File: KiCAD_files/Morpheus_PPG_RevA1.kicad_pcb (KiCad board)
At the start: 2 copper layers, 52.8 x 29.7 mm, 33 parts, among them P1 CONN_01X01, P10 CONN_01X04, P11 CONN_01X01, P12 CONN_01X04, P13 CONN_01X01, P14 CONN_01X01, P2 CONN_01X01, P3 CONN_01X01, P4 CONN_01X01, P5 CONN_01X01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

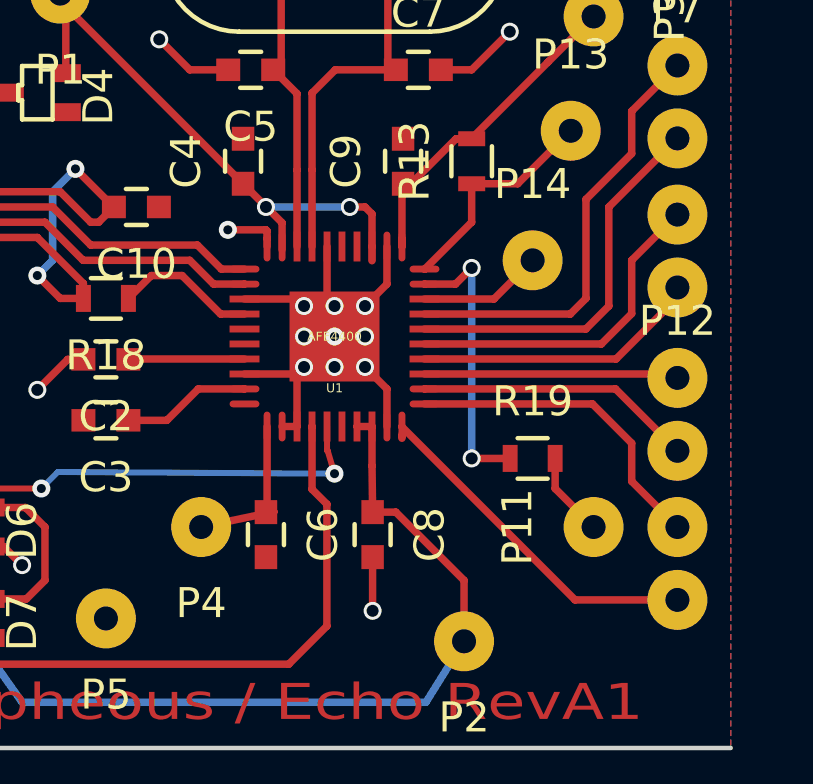
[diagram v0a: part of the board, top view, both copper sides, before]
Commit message: Copper traces for silk screen
Minor corrections (GND) + alignment traces on the corners of AFE4400
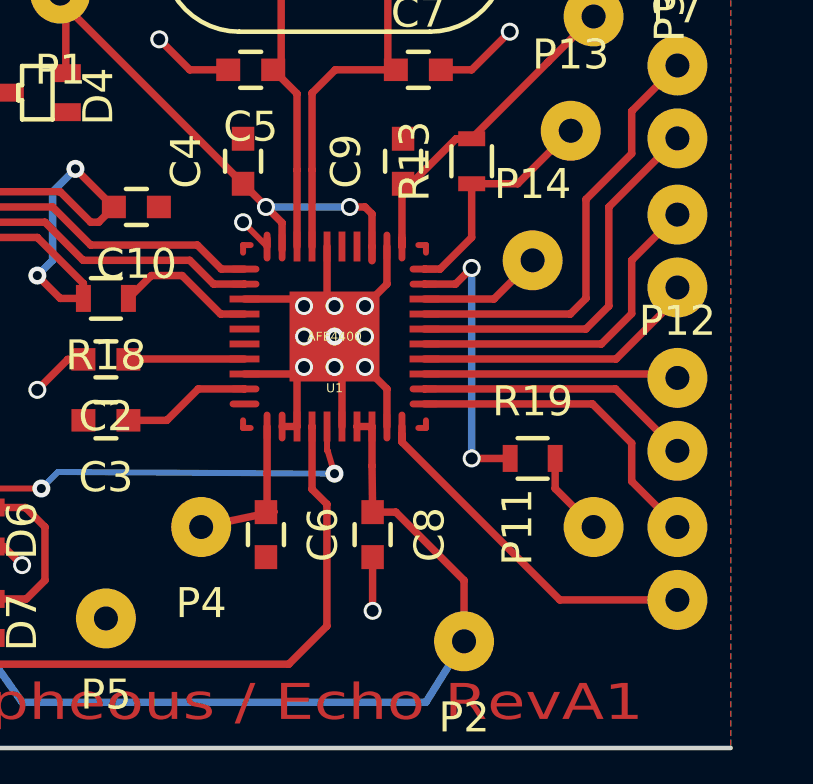
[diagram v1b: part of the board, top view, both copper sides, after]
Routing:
- net GND: track 41.5 -> 44.2 mm
- net (no net): track 8.83 -> 10.9 mm
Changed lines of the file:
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@@
     (thickness 1.6)
     (drawings 15)
-    (tracks 391)
+    (tracks 400)
     (zones 0)
     (modules 33)
@@
       (padsonsilk false)
       (subtractmaskfromsilk false)
-      (outputformat 1)
+      (outputformat 4)
       (mirror false)
       (drillshape 0)
@@
     (effects (font (size 1.5 1.5) (thickness 0.3)))
   )
+  (segment (start 145.542 103.124) (end 145.542 102.87) (width 0.2) (layer F.Cu) (net 0))
+  (segment (start 145.542 102.87) (end 145.288 102.87) (width 0.2) (layer F.Cu) (net 0))
+  (segment (start 145.288 108.966) (end 145.542 108.966) (width 0.2) (layer F.Cu) (net 0))
+  (segment (start 145.542 108.966) (end 145.542 108.712) (width 0.2) (layer F.Cu) (net 0))
   (segment (start 105.58 102.832) (end 104.94 102.832) (width 0.25) (layer F.Cu) (net 0))
   (segment (start 104.902 105.664) (end 104.902 106.172) (width 0.25) (layer F.Cu) (net 0))
@@
   (segment (start 139.4942 108.166) (end 139.4943 108.1659) (width 0.2) (layer F.Cu) (net 0) (status 30))
   (segment (start 139.494 108.166) (end 139.4942 108.166) (width 0.2) (layer F.Cu) (net 0) (status 30))
+  (segment (start 139.7 108.966) (end 139.446 108.966) (width 0.2) (layer F.Cu) (net 0))
+  (segment (start 139.446 108.966) (end 139.446 108.712) (width 0.2) (layer F.Cu) (net 0))
+  (segment (start 139.446 103.124) (end 139.446 102.87) (width 0.2) (layer F.Cu) (net 0))
+  (segment (start 139.446 102.87) (end 139.7 102.87) (width 0.2) (layer F.Cu) (net 0))
   (segment (start 139.49426 106.6673) (end 135.6367 106.6673) (width 0.25) (layer F.Cu) (net 1))
   (segment (start 135.6367 106.6673) (end 135.624 106.68) (width 0.25) (layer F.Cu) (net 1))
   (segment (start 139.494 106.667) (end 139.4943 106.6673) (width 0.2) (layer F.Cu) (net 1) (status 30))
-  (segment (start 130.99796 112.91824) (end 131.46024 112.91824) (width 0.25) (layer F.Cu) (net 2) (status C00000))
-  (segment (start 131.46024 112.91824) (end 132.08 113.538) (width 0.25) (layer F.Cu) (net 2) (status 400000))
+  (segment (start 140.2461 102.91826) (end 139.49426 102.15626) (width 0.2) (layer F.Cu) (net 2))
+  (via (at 139.446 102.108) (size 0.6) (drill 0.4) (layers F.Cu B.Cu) (net 2))
+  (segment (start 139.49426 102.15626) (end 139.446 102.108) (width 0.2) (layer F.Cu) (net 2))
+  (segment (start 142.74292 108.91774) (end 142.74292 106.16692) (width 0.25) (layer F.Cu) (net 2))
+  (segment (start 142.74292 106.16692) (end 142.494 105.918) (width 0.25) (layer F.Cu) (net 2))
+  (segment (start 130.99796 112.91824) (end 131.46024 112.91824) (width 0.25) (layer F.Cu) (net 2))
+  (segment (start 131.46024 112.91824) (end 132.08 113.538) (width 0.25) (layer F.Cu) (net 2))
   (via (at 132.08 113.538) (size 0.6) (drill 0.4) (layers F.Cu B.Cu) (net 2))
   (segment (start 134.124 106.68) (end 133.604 106.68) (width 0.25) (layer F.Cu) (net 2))
@@
   (via (at 141.478 104.902) (size 0.6) (drill 0.4) (layers F.Cu B.Cu) (net 2) (status 30))
   (segment (start 141.478 104.902) (end 142.494 105.918) (width 0.25) (layer F.Cu) (net 2) (status 30))
-  (via (at 138.938 102.362) (size 0.6) (layers F.Cu B.Cu) (net 2))
   (via (at 142.494 105.918) (size 0.6) (layers F.Cu B.Cu) (net 2) (status 30))
-  (segment (start 140.208 102.362) (end 138.938 102.362) (width 0.25) (layer F.Cu) (net 2))
-  (segment (start 140.246 102.4) (end 140.208 102.362) (width 0.25) (layer F.Cu) (net 2))
-  (segment (start 140.246 102.654) (end 140.246 102.4) (width 0.25) (layer F.Cu) (net 2) (status 10))
   (segment (start 140.246 102.918) (end 140.246 102.654) (width 0.2) (layer F.Cu) (net 2) (status 30))
   (segment (start 142.743 106.167) (end 142.494 105.918) (width 0.25) (layer F.Cu) (net 2) (status 30))
@@
   (segment (start 141.7447 100.3608) (end 141.7447 102.9183) (width 0.2) (layer F.Cu) (net 7) (status 20))
   (segment (start 141.745 100.3605) (end 141.7447 100.3608) (width 0.2) (layer F.Cu) (net 7))
-  (segment (start 130.99796 111.61776) (end 132.19176 111.61776) (width 0.25) (layer F.Cu) (net 8) (status 400000))
-  (segment (start 132.22224 114.66576) (end 130.99796 114.66576) (width 0.25) (layer F.Cu) (net 8) (status 800000))
+  (segment (start 130.99796 111.61776) (end 132.19176 111.61776) (width 0.25) (layer F.Cu) (net 8))
+  (segment (start 132.22224 114.66576) (end 130.99796 114.66576) (width 0.25) (layer F.Cu) (net 8))
   (segment (start 132.842 114.046) (end 132.22224 114.66576) (width 0.25) (layer F.Cu) (net 8))
   (segment (start 132.842 112.268) (end 132.842 114.046) (width 0.25) (layer F.Cu) (net 8))
@@
   (segment (start 153.924 104.902) (end 153.924 104.538) (width 0.25) (layer F.Cu) (net 14) (status 30))
   (segment (start 145.494 106.667) (end 145.4937 106.6673) (width 0.2) (layer F.Cu) (net 14) (status 30))
+  (segment (start 145.49374 103.6701) (end 146.0119 103.6701) (width 0.25) (layer F.Cu) (net 15))
+  (segment (start 147.066 102.616) (end 147.066 100.826) (width 0.25) (layer F.Cu) (net 15))
+  (segment (start 146.0119 103.6701) (end 147.066 102.616) (width 0.25) (layer F.Cu) (net 15))
   (segment (start 147.066 100.826) (end 148.602 100.826) (width 0.25) (layer F.Cu) (net 15))
   (segment (start 148.602 100.826) (end 150.368 99.06) (width 0.25) (layer F.Cu) (net 15) (status 20))
   (segment (start 145.49374 103.6701) (end 145.5039 103.6701) (width 0.25) (layer F.Cu) (net 15))
-  (segment (start 145.5039 103.6701) (end 147.066 102.108) (width 0.25) (layer F.Cu) (net 15))
-  (segment (start 147.066 102.108) (end 147.066 100.826) (width 0.25) (layer F.Cu) (net 15))
   (segment (start 145.494 103.67) (end 145.504 103.67) (width 0.25) (layer F.Cu) (net 15) (status 30))
   (segment (start 145.4938 103.67) (end 145.4937 103.6701) (width 0.2) (layer F.Cu) (net 15) (status 30))
@@
   (segment (start 151.0919 108.1659) (end 152.4 109.474) (width 0.25) (layer F.Cu) (net 19))
   (segment (start 153.67 112.522) (end 153.924 112.268) (width 0.25) (layer F.Cu) (net 19) (status 30))
-  (segment (start 144.7419 108.91774) (end 144.7419 108.9279) (width 0.25) (layer F.Cu) (net 20))
-  (segment (start 144.7419 108.9279) (end 150.512 114.698) (width 0.25) (layer F.Cu) (net 20))
-  (segment (start 150.512 114.698) (end 153.924 114.698) (width 0.25) (layer F.Cu) (net 20))
+  (segment (start 144.7419 108.91774) (end 144.7419 109.4359) (width 0.25) (layer F.Cu) (net 20))
+  (segment (start 150.004 114.698) (end 153.924 114.698) (width 0.25) (layer F.Cu) (net 20))
+  (segment (start 144.7419 109.4359) (end 150.004 114.698) (width 0.25) (layer F.Cu) (net 20))
   (segment (start 144.742 109.309) (end 144.742 109.2455) (width 0.25) (layer F.Cu) (net 20) (status 30))
   (segment (start 144.742 109.2455) (end 144.742 109.182) (width 0.25) (layer F.Cu) (net 20) (status 30))
-  (segment (start 144.7419 109.2454) (end 144.7419 108.9177) (width 0.2) (layer F.Cu) (net 20) (status 30))
   (segment (start 144.742 109.2455) (end 144.7419 109.2454) (width 0.2) (layer F.Cu) (net 20) (status 30))
   (via (at 133.858 100.33) (size 0.6) (layers F.Cu B.Cu) (net 21))
@@
   (via (at 107.442 112.014) (size 0.6) (drill 0.4) (layers F.Cu B.Cu) (net 27))
   (segment (start 107.58 111.876) (end 107.442 112.014) (width 0.25) (layer B.Cu) (net 27))
-  (segment (start 129.09804 112.268) (end 127.462 112.268) (width 0.25) (layer F.Cu) (net 28) (status C00000))
-  (segment (start 127.462 112.268) (end 127.038 112.692) (width 0.25) (layer F.Cu) (net 28) (status C00000))
-  (segment (start 127.038 112.692) (end 125.438 112.692) (width 0.25) (layer F.Cu) (net 28) (status C00000))
+  (segment (start 129.09804 112.268) (end 127.462 112.268) (width 0.25) (layer F.Cu) (net 28))
+  (segment (start 127.462 112.268) (end 127.038 112.692) (width 0.25) (layer F.Cu) (net 28))
+  (segment (start 127.038 112.692) (end 125.438 112.692) (width 0.25) (layer F.Cu) (net 28))
   (via (at 132.722 110.9844) (size 0.6) (layers F.Cu B.Cu) (net 28))
   (segment (start 129.0977 112.268) (end 130.3813 110.9844) (width 0.2) (layer F.Cu) (net 28) (status 10))
@@
   (segment (start 129.0977 112.268) (end 129.0973 112.268) (width 0.25) (layer F.Cu) (net 28) (status 30))
   (segment (start 129.0977 112.268) (end 129.0973 112.268) (width 0.25) (layer F.Cu) (net 28) (status 30))
-  (segment (start 129.09804 115.316) (end 127.462 115.316) (width 0.25) (layer F.Cu) (net 29) (status C00000))
-  (segment (start 127.462 115.316) (end 127.038 114.892) (width 0.25) (layer F.Cu) (net 29) (status C00000))
-  (segment (start 127.038 114.892) (end 125.438 114.892) (width 0.25) (layer F.Cu) (net 29) (status C00000))
+  (segment (start 129.09804 115.316) (end 127.462 115.316) (width 0.25) (layer F.Cu) (net 29))
+  (segment (start 127.462 115.316) (end 127.038 114.892) (width 0.25) (layer F.Cu) (net 29))
+  (segment (start 127.038 114.892) (end 125.438 114.892) (width 0.25) (layer F.Cu) (net 29))
   (segment (start 142.24 115.57) (end 142.24 111.506) (width 0.25) (layer F.Cu) (net 29))
   (segment (start 129.09804 116.39804) (end 129.54 116.84) (width 0.25) (layer F.Cu) (net 29))
